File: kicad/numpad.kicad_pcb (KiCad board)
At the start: 2 copper layers, 76.5 x 114.5 mm, 53 parts

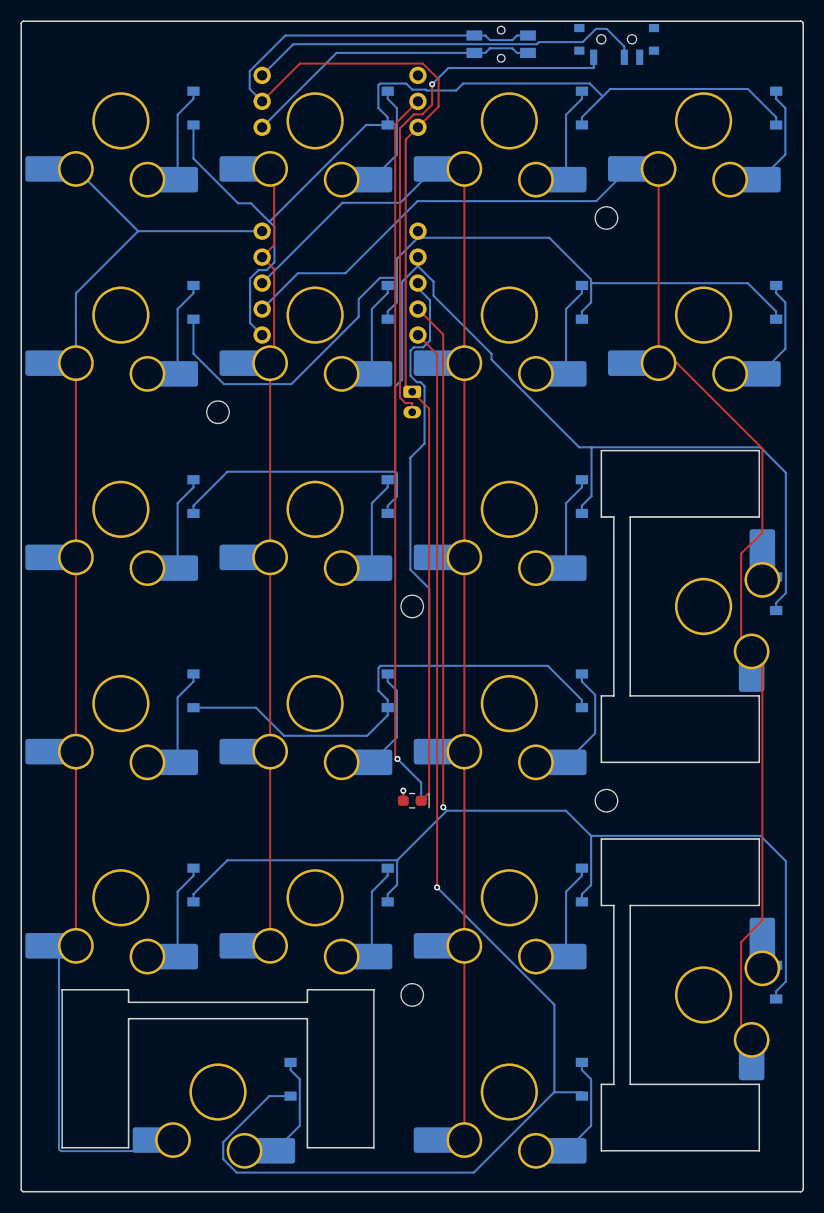
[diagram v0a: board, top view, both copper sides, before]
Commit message: Move nice!nano 1.5mm to the edge, add its CAD model, USB scoop
- nice!nano v2 STEP (kicad/3d/) is now the authority for the case's nano
  and USB-C geometry, and the MCU footprint's 3D model (rotate -90,
  offset 0.11/2.45, verified by exporting the board to STEP).
- MCU moved 1.5mm toward the top edge (KiCad y 13.25 -> 11.75): nano edge
  flush with the PCB edge, USB-C 0.96 past it. Pin clearance improves to
  >=1.51. Re-routed (RAW re-routed alone after freerouting ran it over a
  PWR1 no-net pad); DRC 0 errors, 0 unconnected.
- Case: USB window from the CAD model with 0.25 clearance, a 12.5x6.5 r1.5
  cable-head scoop whose back wall is flush with the USB mouth (collar
  inside the cavity only when the mouth sits behind the wall).
- Fab: kicad/scripts/export_all.sh regenerates fab/, the PCBWay package
  and the board renders; both recipes reproduce the 2026-10-01 exports of
  the old board. All outputs regenerated for the new board.

Co-Authored-By: Claude Opus 5.5 <noreply@anthropic.com>
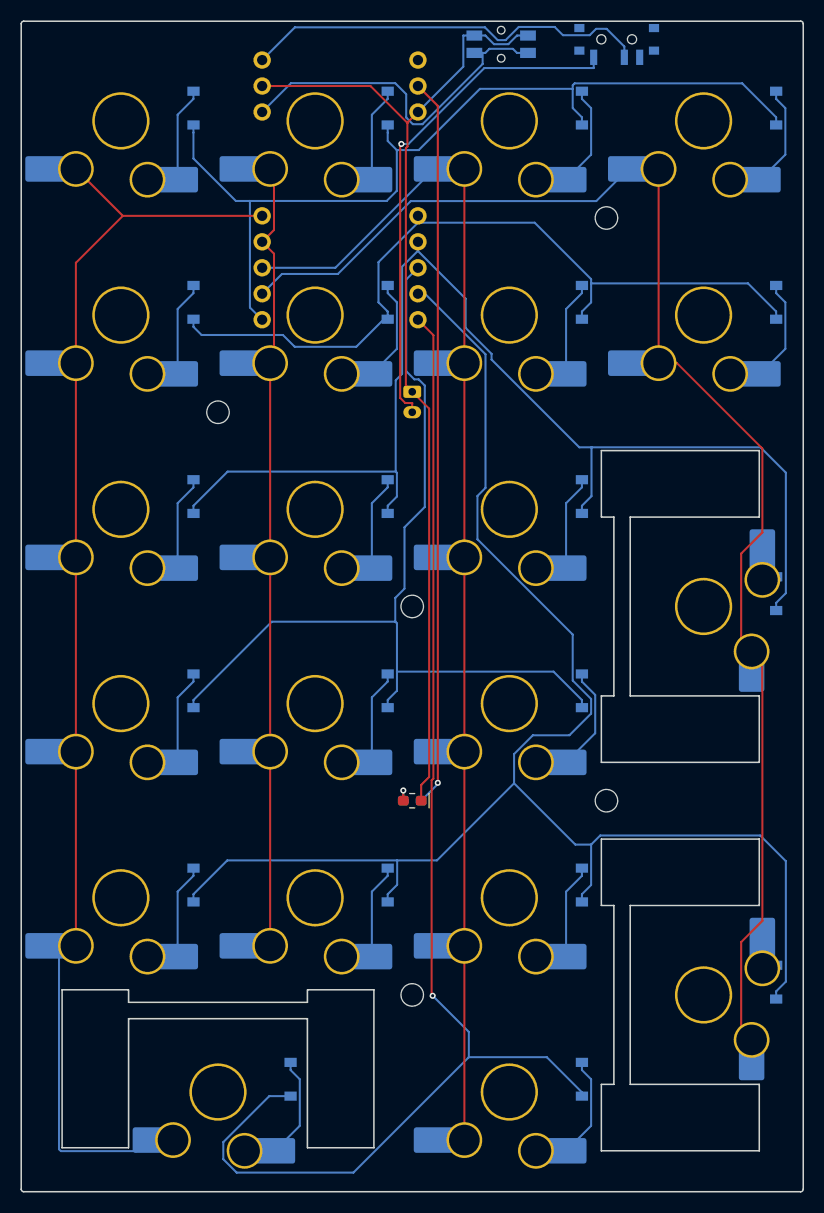
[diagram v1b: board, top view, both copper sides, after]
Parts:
- moved MCU1 1.50 mm to (121.4, 11.8)
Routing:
- net GND: track 125.1 -> 101.2 mm
- net R5: track 139.5 -> 152.6 mm, vias 1 -> 0
- net RST: track 29.4 -> 34.8 mm
- net R2: track 82.5 -> 77.4 mm
- net R3: track 114.6 -> 117.5 mm
- net R6: track 129.0 -> 126.6 mm
- net BAT_P: track 52.3 -> 50.1 mm
- net R1: track 92.2 -> 90.3 mm
- net RAW: track 39.1 -> 40.2 mm
- net P0: track 70.4 -> 71.4 mm
- net c3_r1: track 12.2 -> 13.0 mm
- net c2_r2: track 12.2 -> 13.0 mm
- net c2_r1: track 13.0 -> 12.2 mm
- net c2_r4: track 13.0 -> 12.2 mm
- net C3: track 134.2 -> 133.5 mm
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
